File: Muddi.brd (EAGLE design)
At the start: 106.3 x 85 mm, 13 parts, among them IC1 7805TV, J1 DCJ0202

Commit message: Use MAX811 for Reset. Add Power Capacitors.
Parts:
- added C1: 100nF, capacitor-wima:C2.5-2
- added C2: 33uF, rcl:E2,5-7
- added MAX811: MAX811, jean:SOT143
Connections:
- new net N$27: MAX811.3, S1.1, S1.2
- net GND: now also C1.2, C2.-, MAX811.1
- net N$26: now also C2.+
- net N$40: now also MAX811.2; no longer S1.1, S1.2
- net VCC: now also C1.1, MAX811.4
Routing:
- net VCC: track 129.2 -> 148.2 mm
- net N$27: track 0.00 -> 11.9 mm
- net N$40: track 91.6 -> 80.3 mm
- net N$26: track 19.6 -> 27.2 mm
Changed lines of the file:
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@@
 <element name="U$1" library="bfl" package="OSHW1" value="" x="56.7436" y="6.604"/>
 <element name="IC1" library="linear" package="TO220V" value="7805TV" x="22.86" y="10.16"/>
+<element name="MAX811" library="jean" package="SOT143" value="MAX811" x="92.329" y="15.621" rot="MR180"/>
+<element name="C1" library="capacitor-wima" package="C2.5-2" value="100nF" x="31.75" y="8.89"/>
+<element name="C2" library="rcl" package="E2,5-7" value="33uF" x="21.59" y="15.24"/>
 </elements>
 <signals>
@@
 <contactref element="JP5" pad="79"/>
 <contactref element="JP6" pad="79"/>
-<contactref element="S1" pad="1"/>
-<contactref element="S1" pad="2"/>
 <wire x1="103.73" y1="23.69" x2="101.66" y2="21.62" width="0.254" layer="16"/>
 <wire x1="103.73" y1="24.38" x2="103.73" y2="23.69" width="0.254" layer="16"/>
@@
 <wire x1="103.5" y1="65.55" x2="103.73" y2="65.78" width="0.254" layer="16"/>
 <wire x1="101.66" y1="78.66" x2="101.6" y2="78.74" width="0.254" layer="16"/>
-<wire x1="100.8126" y1="9.6012" x2="94.4118" y2="9.6012" width="0.254" layer="16"/>
-<wire x1="94.4118" y1="9.6012" x2="94.4118" y2="9.6266" width="0.254" layer="16"/>
-<wire x1="100.8126" y1="9.6012" x2="100.9142" y2="9.6266" width="0.254" layer="16"/>
-<wire x1="98.5012" y1="19.7612" x2="98.5012" y2="11.0998" width="0.254" layer="16"/>
-<wire x1="101.6" y1="21.59" x2="98.5012" y2="19.7612" width="0.254" layer="16"/>
-<wire x1="98.5012" y1="11.0998" x2="100.9142" y2="9.6266" width="0.254" layer="16"/>
+<contactref element="MAX811" pad="2"/>
+<wire x1="96.9264" y1="16.9164" x2="93.4974" y2="16.9164" width="0.254" layer="16"/>
+<wire x1="101.6" y1="21.59" x2="96.9264" y2="16.9164" width="0.254" layer="16"/>
+<wire x1="93.4974" y1="16.9164" x2="93.279" y2="16.721" width="0.254" layer="16"/>
 </signal>
 <signal name="N$41">
@@
 <wire x1="76.1238" y1="14.1732" x2="76.2" y2="13.97" width="0.254" layer="16"/>
 <wire x1="68.58" y1="21.717" x2="68.58" y2="21.59" width="0.254" layer="16"/>
-<wire x1="51.435" y1="5.2578" x2="25.4" y2="5.2578" width="0.254" layer="16"/>
+<wire x1="51.435" y1="5.2578" x2="30.4038" y2="5.2578" width="0.254" layer="16"/>
+<wire x1="30.4038" y1="5.2578" x2="25.4" y2="5.2578" width="0.254" layer="16"/>
 <wire x1="68.1228" y1="21.9456" x2="51.435" y2="5.2578" width="0.254" layer="16"/>
 <wire x1="25.4" y1="5.2578" x2="25.4" y2="7.62" width="0.254" layer="16"/>
 <wire x1="68.1228" y1="21.9456" x2="68.58" y2="21.59" width="0.254" layer="16"/>
+<contactref element="MAX811" pad="4"/>
+<contactref element="C1" pad="1"/>
+<wire x1="76.581" y1="14.4018" x2="91.2114" y2="14.4018" width="0.254" layer="16"/>
+<wire x1="76.3524" y1="14.1732" x2="76.581" y2="14.4018" width="0.254" layer="16"/>
+<wire x1="91.2114" y1="14.4018" x2="91.379" y2="14.521" width="0.254" layer="16"/>
+<wire x1="76.3524" y1="14.1732" x2="76.2" y2="13.97" width="0.254" layer="16"/>
+<wire x1="30.4038" y1="5.2578" x2="30.4038" y2="8.6868" width="0.254" layer="16"/>
+<wire x1="30.4038" y1="8.6868" x2="30.48" y2="8.89" width="0.254" layer="16"/>
 </signal>
 <signal name="GND">
@@
 <contactref element="JP6" pad="78"/>
 <contactref element="JP6" pad="80"/>
+<contactref element="MAX811" pad="1"/>
+<contactref element="C2" pad="-"/>
+<contactref element="C1" pad="2"/>
 </signal>
 <signal name="N$25">
@@
 <wire x1="10.5156" y1="7.6708" x2="13.26" y2="7.62" width="0.254" layer="16"/>
 <wire x1="13.26" y1="7.62" x2="20.32" y2="7.62" width="0.4064" layer="16"/>
+<contactref element="C2" pad="+"/>
+<wire x1="20.3454" y1="7.7724" x2="20.3454" y2="15.0876" width="0.254" layer="16"/>
+<wire x1="20.3454" y1="15.0876" x2="20.32" y2="15.24" width="0.254" layer="16"/>
+<wire x1="20.3454" y1="7.7724" x2="20.32" y2="7.62" width="0.254" layer="16"/>
+</signal>
+<signal name="N$27">
+<contactref element="S1" pad="1"/>
+<contactref element="S1" pad="2"/>
+<wire x1="100.8126" y1="9.6012" x2="94.4118" y2="9.6012" width="0.254" layer="16"/>
+<wire x1="94.4118" y1="9.6012" x2="94.4118" y2="9.6266" width="0.254" layer="16"/>
+<wire x1="100.8126" y1="9.6012" x2="100.9142" y2="9.6266" width="0.254" layer="16"/>
+<contactref element="MAX811" pad="3"/>
+<wire x1="93.4974" y1="10.7442" x2="93.4974" y2="14.4018" width="0.254" layer="16"/>
+<wire x1="94.4118" y1="9.8298" x2="93.4974" y2="10.7442" width="0.254" layer="16"/>
+<wire x1="93.4974" y1="14.4018" x2="93.279" y2="14.521" width="0.254" layer="16"/>
+<wire x1="94.4118" y1="9.8298" x2="94.4118" y2="9.6266" width="0.254" layer="16"/>
 </signal>
 </signals>

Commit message: Fix Memory Mapping inversely. Move Text on Muddi
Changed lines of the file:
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@@
 <wire x1="105" y1="85" x2="-1.27" y2="85" width="0" layer="20"/>
 <wire x1="-1.27" y1="85" x2="-1.27" y2="0" width="0" layer="20"/>
-<text x="30.48" y="12.7" size="1.778" layer="21" font="fixed">CPD-80 MUDDI v1</text>
+<text x="33.02" y="15.24" size="1.778" layer="21" font="fixed">CPD-80 MUDDI v1</text>
 <rectangle x1="38.1381" y1="1.8161" x2="38.4683" y2="1.8415" layer="21"/>
 <rectangle x1="37.9349" y1="1.8415" x2="38.5445" y2="1.8669" layer="21"/>
@@
 <rectangle x1="38.6461" y1="6.3881" x2="38.7731" y2="6.4135" layer="21"/>
 <rectangle x1="38.6461" y1="6.4135" x2="38.7731" y2="6.4389" layer="21"/>
-<text x="48.26" y="11.43" size="1.778" layer="21" font="fixed" rot="R180">2017 jhbruhn</text>
+<text x="52.832" y="14.097" size="1.778" layer="21" font="fixed" rot="R180">2017 jhbruhn</text>
 <hole x="1.27" y="17.78" drill="2"/>
 <hole x="102.87" y="17.78" drill="2"/>

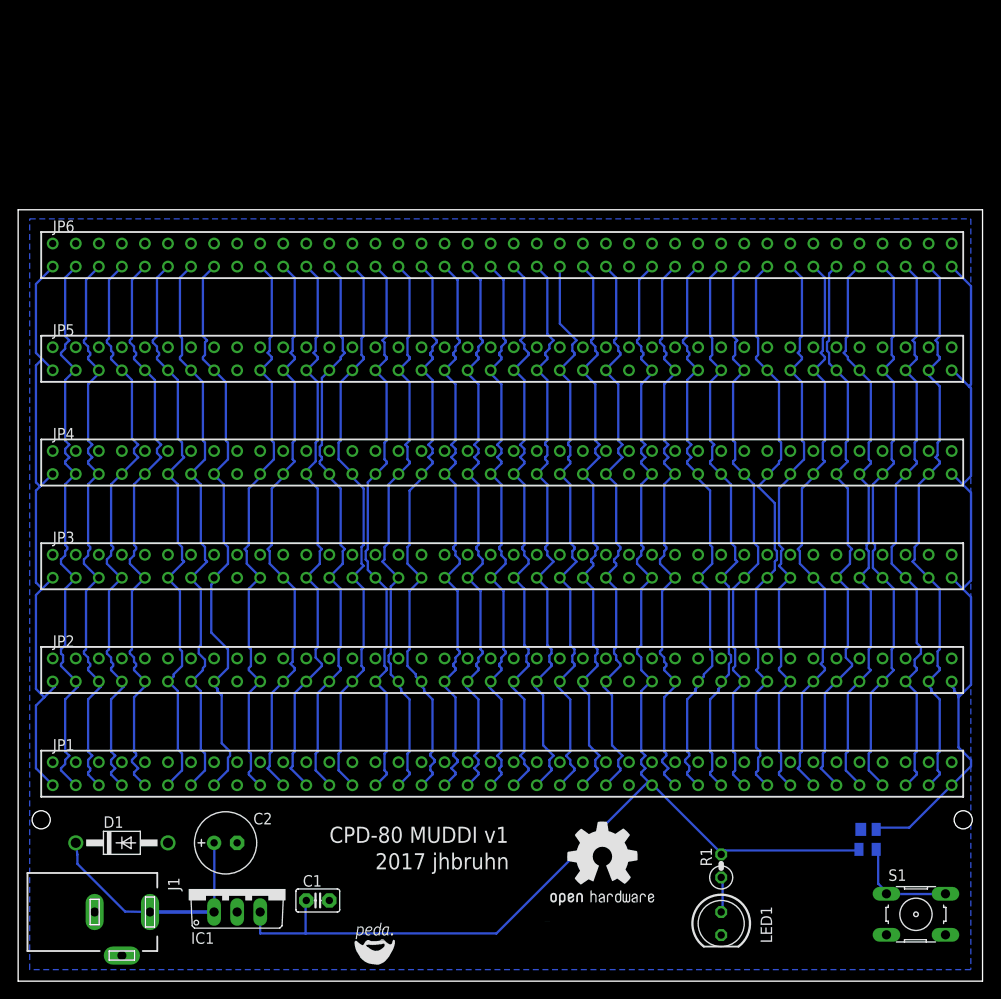
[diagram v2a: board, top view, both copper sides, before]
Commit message: Update Muddi Spacing
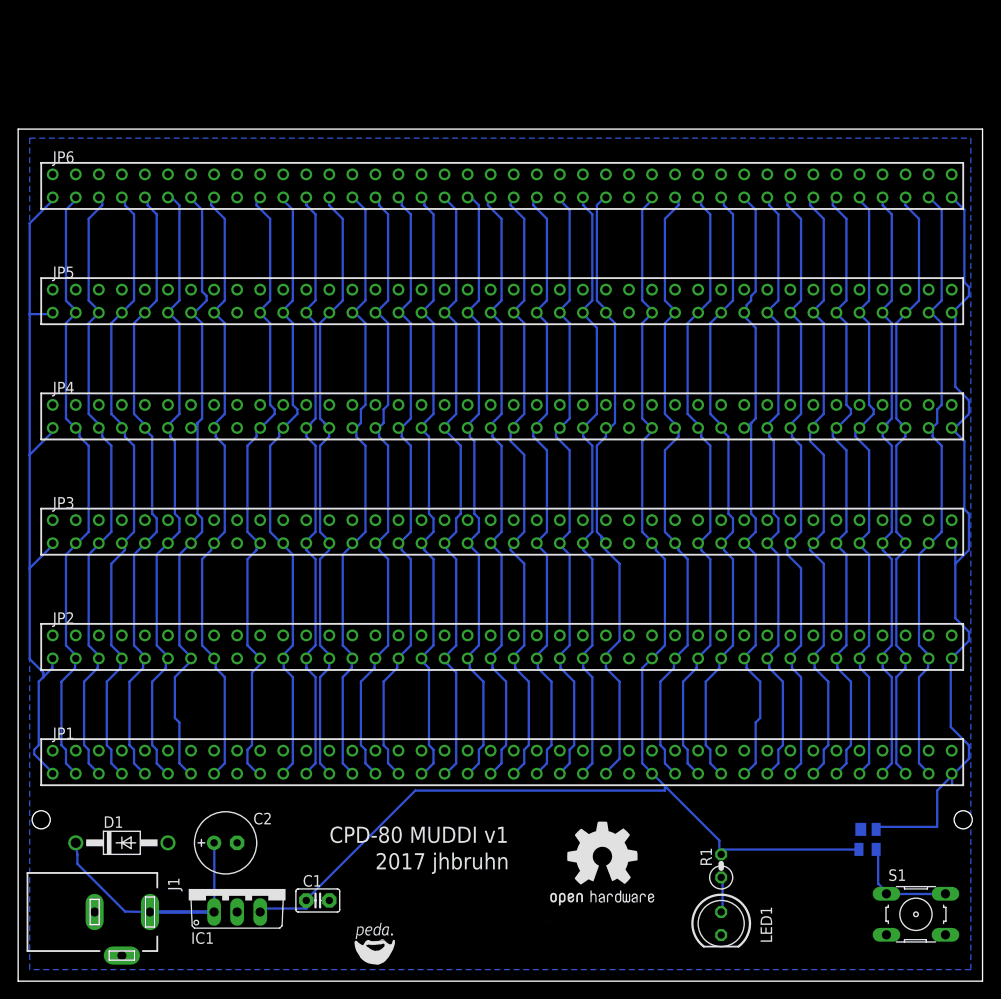
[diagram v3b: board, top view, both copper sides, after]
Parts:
- moved JP6 7.62 mm to (11.4, 87.6)
- moved JP5 6.35 mm to (11.4, 74.9)
- moved JP4 5.08 mm to (11.4, 62.2)
- moved JP3 3.81 mm to (11.4, 49.5)
- moved JP2 2.54 mm to (11.4, 36.8)
- moved JP1 1.27 mm to (11.4, 24.1)
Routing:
- net N$1: track 68.8 -> 79.4 mm
- net N$40: track 80.3 -> 88.6 mm
- net N$14: track 63.2 -> 69.9 mm
- net N$15: track 63.5 -> 69.7 mm
- net N$45: track 63.7 -> 69.6 mm
- net N$9: track 64.0 -> 69.8 mm
- net N$46: track 63.6 -> 69.3 mm
- net N$13: track 63.6 -> 69.3 mm
- net N$7: track 64.4 -> 70.0 mm
- net N$38: track 64.0 -> 69.5 mm
- net N$42: track 63.9 -> 69.3 mm
- net N$37: track 64.4 -> 69.5 mm
- net N$41: track 63.5 -> 68.5 mm
- net N$47: track 64.0 -> 68.9 mm
- net N$43: track 63.3 -> 68.1 mm
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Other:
- board size 106.3 x 85 mm -> 106.3 x 93.9 mm

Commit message: Add more mounting holes to muddi
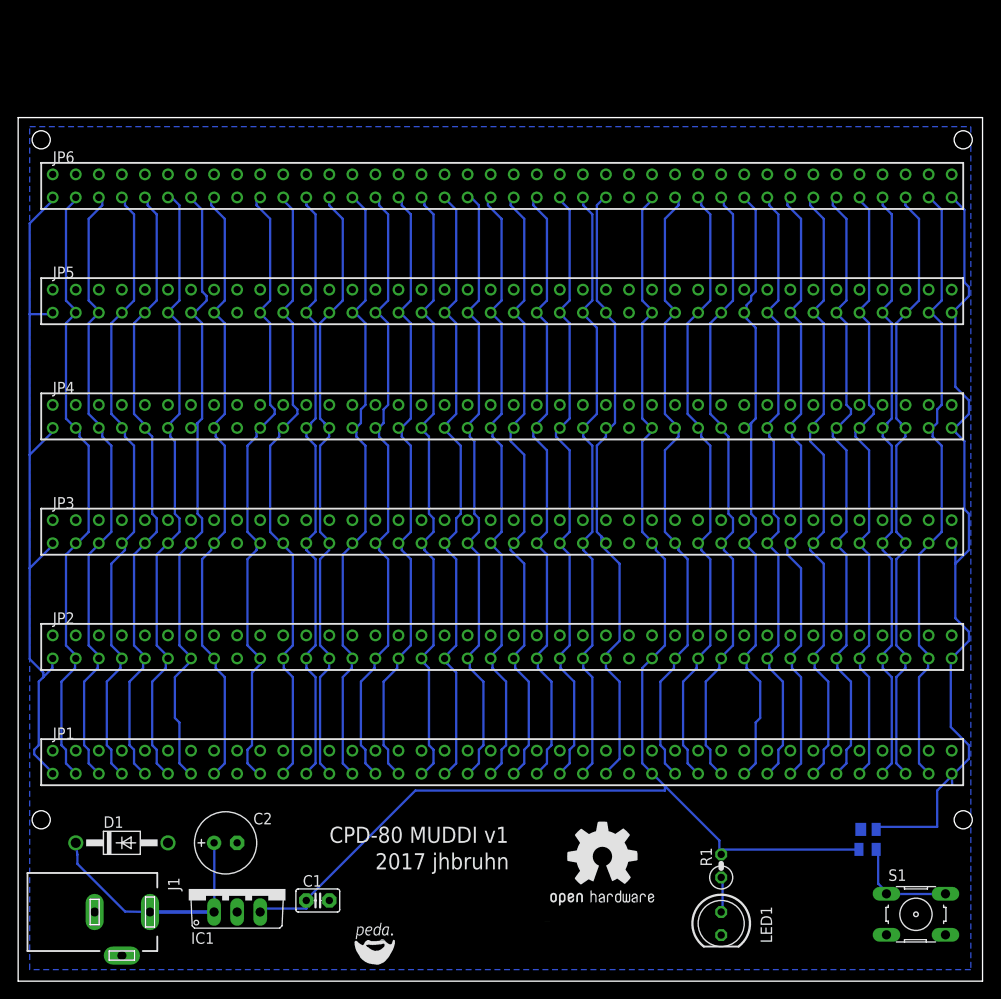
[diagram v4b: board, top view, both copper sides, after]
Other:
- board size 106.3 x 93.9 mm -> 106.3 x 95.2 mm
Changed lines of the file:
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@@
 <plain>
 <wire x1="-1.27" y1="0" x2="105" y2="0" width="0" layer="20"/>
-<wire x1="105" y1="0" x2="105" y2="93.89" width="0" layer="20"/>
-<wire x1="105" y1="93.89" x2="-1.27" y2="93.89" width="0" layer="20"/>
-<wire x1="-1.27" y1="93.89" x2="-1.27" y2="0" width="0" layer="20"/>
+<wire x1="105" y1="0" x2="105" y2="95.16" width="0" layer="20"/>
+<wire x1="105" y1="95.16" x2="-1.27" y2="95.16" width="0" layer="20"/>
+<wire x1="-1.27" y1="95.16" x2="-1.27" y2="0" width="0" layer="20"/>
 <text x="33.02" y="15.24" size="1.778" layer="21" font="fixed">CPD-80 MUDDI v1</text>
 <rectangle x1="38.1381" y1="1.8161" x2="38.4683" y2="1.8415" layer="21"/>
@@
 <hole x="1.27" y="17.78" drill="2"/>
 <hole x="102.87" y="17.78" drill="2"/>
+<hole x="1.27" y="92.71" drill="2"/>
+<hole x="102.87" y="92.71" drill="2"/>
 </plain>
 <attributes>
@@
 <contactref element="JP6" pad="51"/>
 <polygon width="0.254" layer="16" isolate="0.3048">
-<vertex x="0" y="92.89"/>
-<vertex x="103.7082" y="92.89"/>
+<vertex x="0" y="94.16"/>
+<vertex x="103.7082" y="94.16"/>
 <vertex x="103.7082" y="1.27"/>
 <vertex x="0" y="1.27"/>

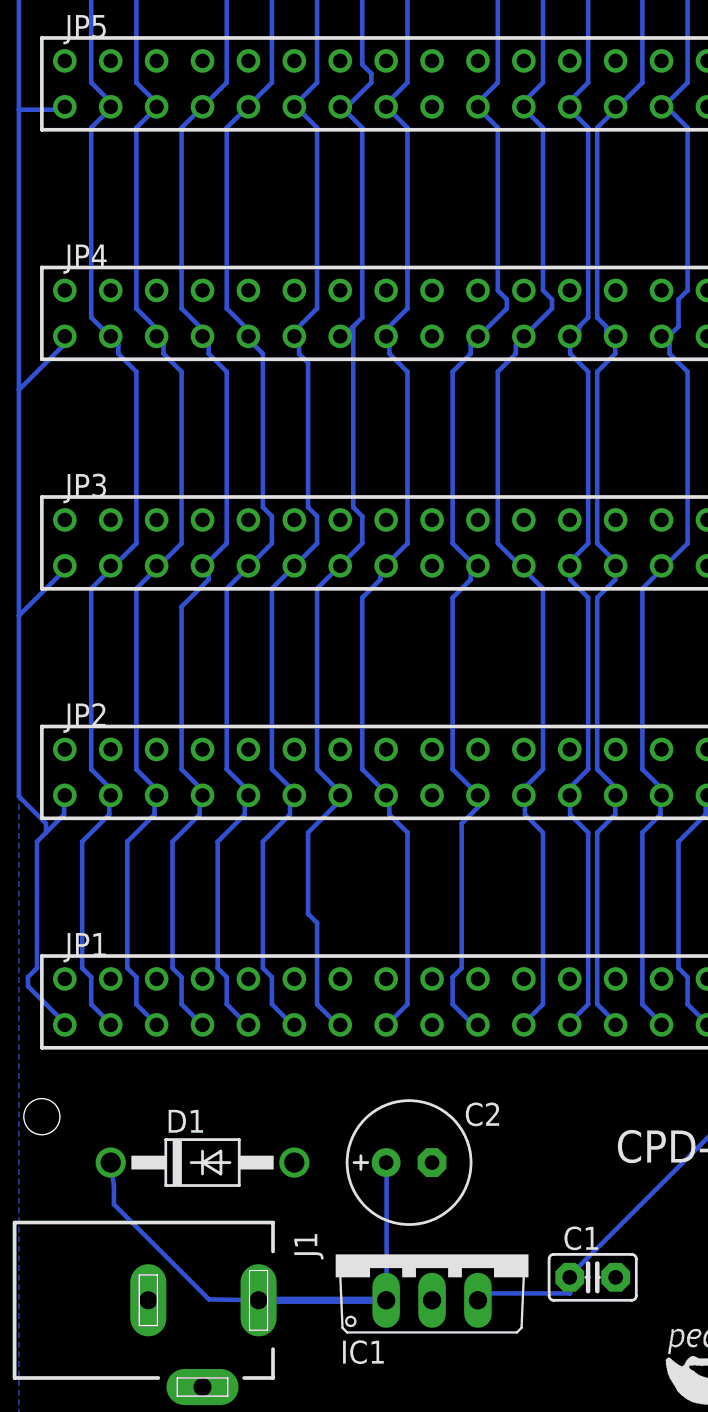
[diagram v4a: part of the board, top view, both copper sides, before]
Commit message: Fix incorrectly connected diode
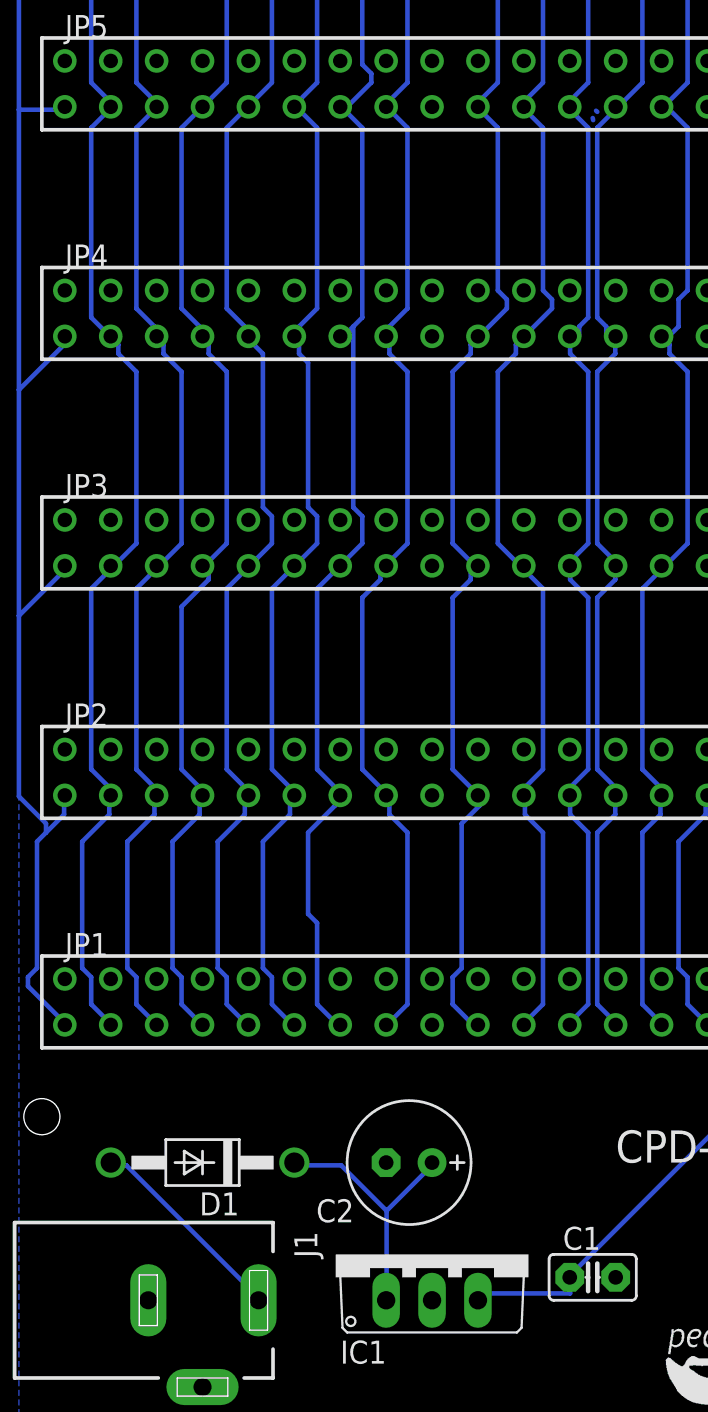
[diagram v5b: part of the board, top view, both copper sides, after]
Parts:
- turned C2 to 180 degrees
- turned D1 to 180 degrees
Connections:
- new net N$28: D1.A, J1.1
- net GND: no longer D1.A
- net N$26: no longer J1.1
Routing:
- net N$26: track 27.2 -> 14.9 mm
- net N$28: track 0.00 -> 11.4 mm
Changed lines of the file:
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@@
 </autorouter>
 <elements>
-<element name="D1" library="diode" package="DO41-10" value="1N4942" x="10.16" y="15.24">
-<attribute name="MPN" value="1N4935G" x="10.16" y="15.24" size="1.778" layer="27" display="off"/>
-<attribute name="MF" value="ON SEMICONDUCTOR" x="10.16" y="15.24" size="1.778" layer="27" display="off"/>
-<attribute name="OC_FARNELL" value="1126305" x="10.16" y="15.24" size="1.778" layer="27" display="off"/>
+<element name="D1" library="diode" package="DO41-10" value="1N4942" x="10.16" y="15.24" rot="R180">
+<attribute name="MPN" value="1N4935G" x="10.16" y="15.24" size="1.778" layer="27" rot="R180" display="off"/>
+<attribute name="MF" value="ON SEMICONDUCTOR" x="10.16" y="15.24" size="1.778" layer="27" rot="R180" display="off"/>
+<attribute name="OC_FARNELL" value="1126305" x="10.16" y="15.24" size="1.778" layer="27" rot="R180" display="off"/>
 </element>
 <element name="J1" library="con-jack" package="DCJ0202" value="DCJ0202" x="10.16" y="7.62" rot="R270">
@@
 <element name="MAX811" library="jean" package="SOT143" value="MAX811" x="92.329" y="15.621" rot="MR180"/>
 <element name="C1" library="capacitor-wima" package="C2.5-2" value="100nF" x="31.75" y="8.89"/>
-<element name="C2" library="rcl" package="E2,5-7" value="33uF" x="21.59" y="15.24"/>
+<element name="C2" library="rcl" package="E2,5-7" value="33uF" x="21.59" y="15.24" rot="R180"/>
 </elements>
 <signals>
@@
 <contactref element="IC1" pad="2"/>
 <contactref element="J1" pad="3"/>
-<contactref element="D1" pad="A"/>
 <contactref element="JP1" pad="2"/>
 <contactref element="JP1" pad="4"/>
@@
 <contactref element="C2" pad="-"/>
 <contactref element="C1" pad="2"/>
+<wire x1="31.7754" y1="72.9234" x2="31.75" y2="73.040259375" width="0.254" layer="16"/>
+<wire x1="32.004" y1="73.3806" x2="31.9342" y2="73.44401875" width="0.254" layer="16"/>
 <wire x1="20.32" y1="76.2" x2="17.78" y2="76.2" width="0" layer="19" extent="1-1"/>
+<wire x1="38.1" y1="63.5" x2="35.56" y2="63.5" width="0" layer="19" extent="1-1"/>
 <wire x1="53.34" y1="50.8" x2="50.8" y2="50.8" width="0" layer="19" extent="1-1"/>
-<wire x1="38.1" y1="63.5" x2="35.56" y2="63.5" width="0" layer="19" extent="1-1"/>
 <wire x1="63.5" y1="63.5" x2="60.96" y2="63.5" width="0" layer="19" extent="1-1"/>
 <wire x1="101.6" y1="63.5" x2="99.06" y2="63.5" width="0" layer="19" extent="1-1"/>
@@
 </signal>
 <signal name="N$26">
-<contactref element="J1" pad="1"/>
 <contactref element="IC1" pad="1"/>
+<contactref element="C2" pad="+"/>
 <contactref element="D1" pad="C"/>
-<wire x1="5.2578" y1="12.9286" x2="5.2578" y2="13.9446" width="0.254" layer="16"/>
-<wire x1="10.5156" y1="7.6708" x2="5.2578" y2="12.9286" width="0.254" layer="16"/>
-<wire x1="5.2578" y1="13.9446" x2="5.08" y2="15.24" width="0.254" layer="16"/>
-<wire x1="10.5156" y1="7.6708" x2="13.26" y2="7.62" width="0.254" layer="16"/>
-<wire x1="13.26" y1="7.62" x2="20.32" y2="7.62" width="0.4064" layer="16"/>
-<contactref element="C2" pad="+"/>
-<wire x1="20.3454" y1="7.7724" x2="20.3454" y2="15.0876" width="0.254" layer="16"/>
-<wire x1="20.3454" y1="15.0876" x2="20.32" y2="15.24" width="0.254" layer="16"/>
+<wire x1="20.3454" y1="12.573" x2="20.3454" y2="7.7724" width="0.254" layer="16"/>
+<wire x1="22.86" y1="15.0876" x2="20.3454" y2="12.573" width="0.254" layer="16"/>
 <wire x1="20.3454" y1="7.7724" x2="20.32" y2="7.62" width="0.254" layer="16"/>
+<wire x1="22.86" y1="15.0876" x2="22.86" y2="15.24" width="0.254" layer="16"/>
+<wire x1="17.8308" y1="15.0876" x2="15.3162" y2="15.0876" width="0.254" layer="16"/>
+<wire x1="20.3454" y1="12.573" x2="17.8308" y2="15.0876" width="0.254" layer="16"/>
+<wire x1="15.3162" y1="15.0876" x2="15.24" y2="15.24" width="0.254" layer="16"/>
 </signal>
 <signal name="N$27">
@@
 <wire x1="94.4118" y1="9.8298" x2="94.4118" y2="9.6266" width="0.254" layer="16"/>
 </signal>
+<signal name="N$28">
+<contactref element="J1" pad="1"/>
+<contactref element="D1" pad="A"/>
+<wire x1="5.9436" y1="15.0876" x2="5.2578" y2="15.0876" width="0.254" layer="16"/>
+<wire x1="13.2588" y1="7.7724" x2="5.9436" y2="15.0876" width="0.254" layer="16"/>
+<wire x1="5.2578" y1="15.0876" x2="5.08" y2="15.24" width="0.254" layer="16"/>
+<wire x1="13.2588" y1="7.7724" x2="13.26" y2="7.62" width="0.254" layer="16"/>
+</signal>
 </signals>
